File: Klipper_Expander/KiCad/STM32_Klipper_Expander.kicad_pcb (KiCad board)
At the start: 2 copper layers, 100 x 24 mm, 47 parts, among them J1 USB_B_Micro, J10 Conn_01x01, J11 Conn_01x03, J12 Conn_01x02, J2 Conn_01x04, J4 Conn_01x03, J5 Vin, J6 Screw_Terminal_01x08, J7 Conn_01x02, J8 Conn_01x02, J9 Conn_01x02, Q1 IRLML6344TRPBF, Q2 IRLML6344TRPBF, Q3 IRLML6344TRPBF, Q4 IRLML6344TRPBF, SW2 SW_SPST, U1 STM32F042F6Px, U2 AP2127K-3.3, U3 74LVC1G17

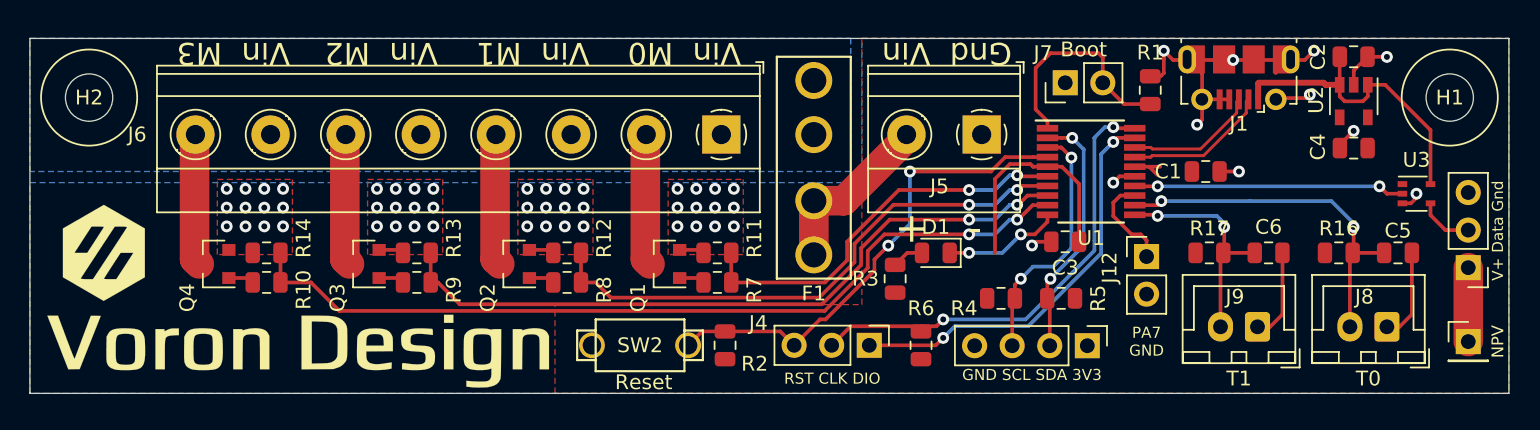
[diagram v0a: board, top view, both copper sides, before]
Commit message: Klipper Expander V2 (#9)
* Status LED's and silkscren adjustments.

Added status LED's for Vin (12/24V), USB (5V), and all 4 mosfets on the drain. LED's will signal mosfet output status.

Gerber and PNP files still need to be completed.

* Updated README to include fuse purchasing options for 2,5,and 10A fuses as well as an assortment.

* Updated Gerber and Production files, Minor changes

Changed thermsitor pullups to 4K7 to increse range and reliability.
Added silkscreen to indicate what the status LED's are showing.

* Conifg and Step additions

Changed onboard LED on PA4 to become a "
Status" LED that will turn on when board is powered and connected.
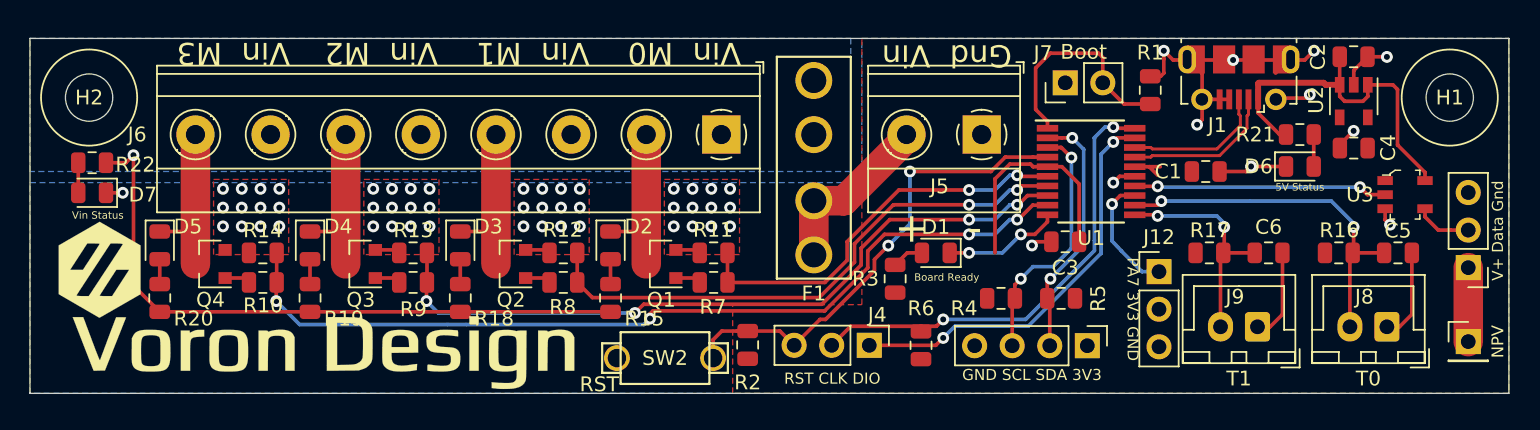
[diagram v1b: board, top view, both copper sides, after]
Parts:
- added D2: LED, LED_SMD:LED_0805_2012Metric, F.Cu at (139.3, 90.0)
- added D3: LED, LED_SMD:LED_0805_2012Metric, F.Cu at (129.1, 90.0)
- added D4: LED, LED_SMD:LED_0805_2012Metric, F.Cu at (118.9, 90.0)
- added D5: LED, LED_SMD:LED_0805_2012Metric, F.Cu at (108.8, 90.0)
- added D6: LED, LED_SMD:LED_0805_2012Metric, F.Cu at (185.9, 84.7)
- added D7: LED, LED_SMD:LED_0805_2012Metric, F.Cu at (104.2, 86.4)
- added R15: 4.7K, Resistor_SMD:R_0805_2012Metric, F.Cu at (139.3, 93.5)
- added R18: 4.7K, Resistor_SMD:R_0805_2012Metric, F.Cu at (129.1, 93.5)
- added R19: 4.7K, Resistor_SMD:R_0805_2012Metric, F.Cu at (118.9, 93.5)
- added R20: 4.7K, Resistor_SMD:R_0805_2012Metric, F.Cu at (108.8, 93.5)
- added R21: 1K, Resistor_SMD:R_0805_2012Metric, F.Cu at (185.9, 82.5)
- added R22: 4.7K, Resistor_SMD:R_0805_2012Metric, F.Cu at (104.2, 84.4)
- J12: value Conn_01x02 -> Conn_01x03; footprint Connector_PinHeader_2.54mm:PinHeader_1x02_P2.54mm_Vertical -> Connector_PinHeader_2.54mm:PinHeader_1x03_P2.54mm_Vertical
- R16, R17: value 10K -> 4.7K
- U3: footprint Package_TO_SOT_SMD:SOT-353_SC-70-5 -> digikey-footprints:SOT-753
- moved SW2 1.90 mm to (142.9, 97.6)
- moved G*** 1.71 mm to (120.0, 96.6)
- moved R2 1.53 mm to (148.5, 96.7)
- moved J12 1.32 mm to (176.3, 91.8)
- moved G*** 1.18 mm to (104.7, 91.6)
- moved U3 0.77 mm to (193.0, 86.6), turned to 270 degrees
- moved Q1 0.25 mm to (142.7, 91.2)
- moved Q2 0.25 mm to (132.5, 91.2)
- moved Q3 0.25 mm to (122.4, 91.2)
- moved Q4 0.25 mm to (112.2, 91.2)
- moved R10 0.25 mm to (115.7, 92.5)
- moved R14 0.25 mm to (115.7, 90.5), turned to 180 degrees
- moved R11 0.25 mm to (146.2, 90.5), turned to 180 degrees
- moved R12 0.25 mm to (136.1, 90.5), turned to 180 degrees
- moved R13 0.25 mm to (125.9, 90.5), turned to 180 degrees
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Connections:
- J12 pad 2: GND -> +3V3
- R11 pad 1: GND -> PWM0
- R11 pad 2: PWM0 -> GND
- R12 pad 1: GND -> PWM1
- R12 pad 2: PWM1 -> GND
- R13 pad 1: GND -> PWM2
- R13 pad 2: PWM2 -> GND
- R14 pad 1: GND -> PWM3
- R14 pad 2: PWM3 -> GND
- R16 pad 1: +3V3 -> T0
- R16 pad 2: T0 -> +3V3
- R17 pad 1: +3V3 -> T1
- R17 pad 2: T1 -> +3V3
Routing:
- net /Vin: track 0.00 -> 43.9 mm, vias 0 -> 1
- net GND: track 52.3 -> 56.6 mm, vias 59 -> 60
- net VCC: track 21.5 -> 24.7 mm
- net Net-(D6-Pad2): track 0.00 -> 2.16 mm
- net /Mosfet0: track 9.02 -> 11.2 mm
- net /Mosfet2: track 9.02 -> 11.2 mm
- net /Mosfet3: track 9.02 -> 11.2 mm
- net /Mosfet1: track 9.02 -> 11.2 mm
- net Net-(D7-Pad2): track 0.00 -> 2.03 mm
- net PWM3: track 58.3 -> 60.3 mm, vias 2 -> 4
- net GPIO: track 6.59 -> 8.33 mm, vias 0 -> 1
- net Net-(D5-Pad2): track 0.00 -> 1.68 mm
- net Net-(D4-Pad2): track 0.00 -> 1.68 mm
- net Net-(D3-Pad2): track 0.00 -> 1.68 mm
- net Net-(D2-Pad2): track 0.00 -> 1.68 mm
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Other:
- board text added: "5V Status"
- board text added: "Board Ready"
- board text added: "PA7 3V3 GND"
- board text added: "RST"
- board text added: "Vin Status"
- board text removed: "PA7 GND"
- board text removed: "Reset"
